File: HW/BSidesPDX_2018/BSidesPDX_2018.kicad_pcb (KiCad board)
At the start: 2 copper layers, 94.7 x 67.7 mm, 46 parts, among them J1 AVR-ISP-6, J2 USB_B_Micro, U1 ATTINY861-15XD, X1 Badgelife_shitty_connector, X2 Badgelife_shitty_connector, X3 Badgelife_shitty_connector, X4 Badgelife_shitty_connector

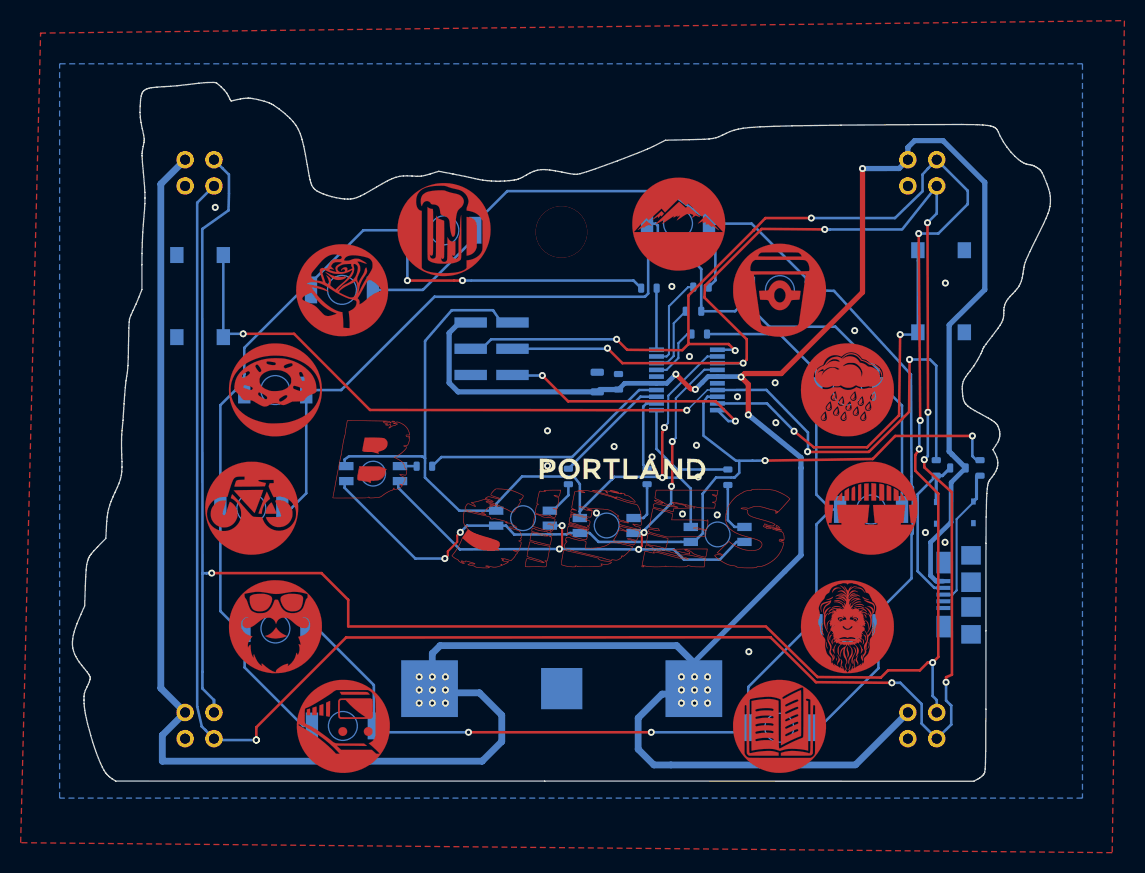
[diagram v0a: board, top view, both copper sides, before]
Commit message: BAD HACK: I edited the txt file of the LED footrpint, then updated all footprints in the schematic, then tweaked a few things. Someone competent should check this!
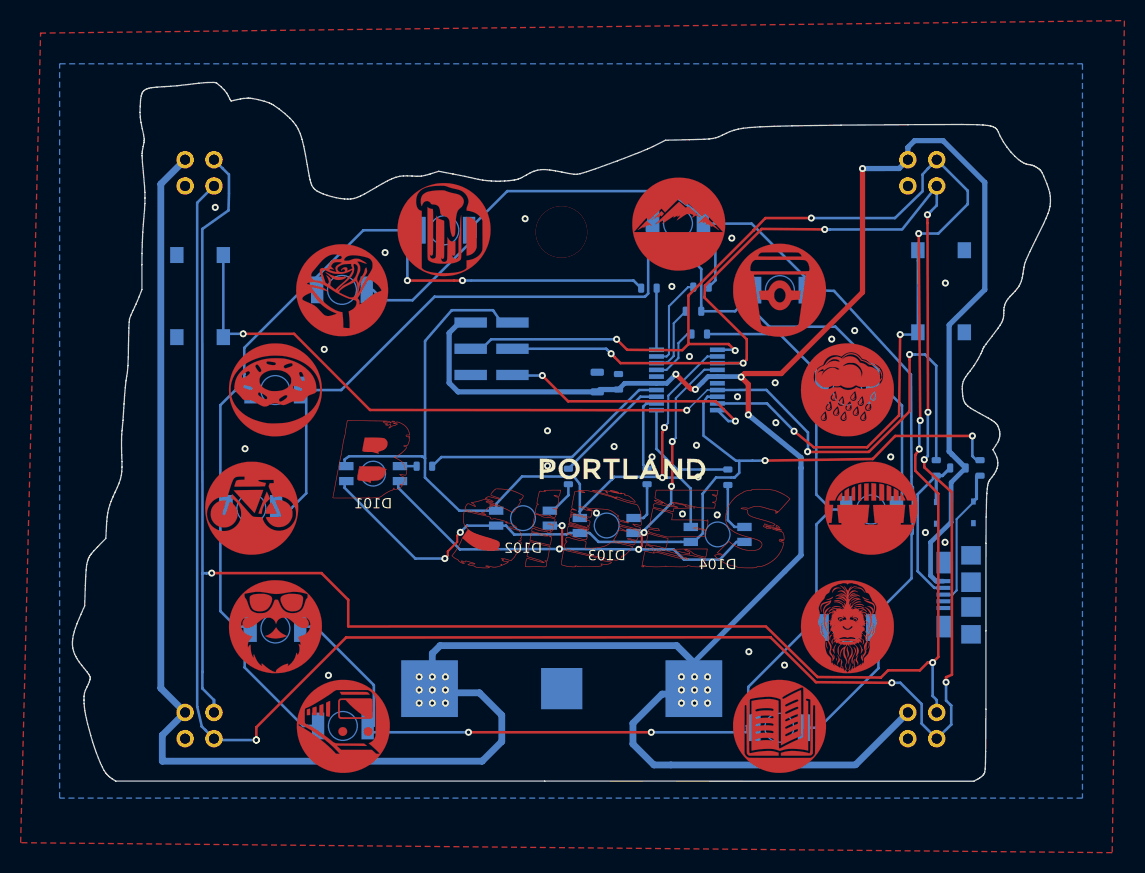
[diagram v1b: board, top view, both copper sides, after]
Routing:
- net /ROW_4: track 101.1 -> 102.3 mm
- net /ROW_2: track 109.7 -> 110.6 mm
- net /L_SWITCH_D-: track 100.8 -> 101.5 mm
- net GND: vias 20 -> 29

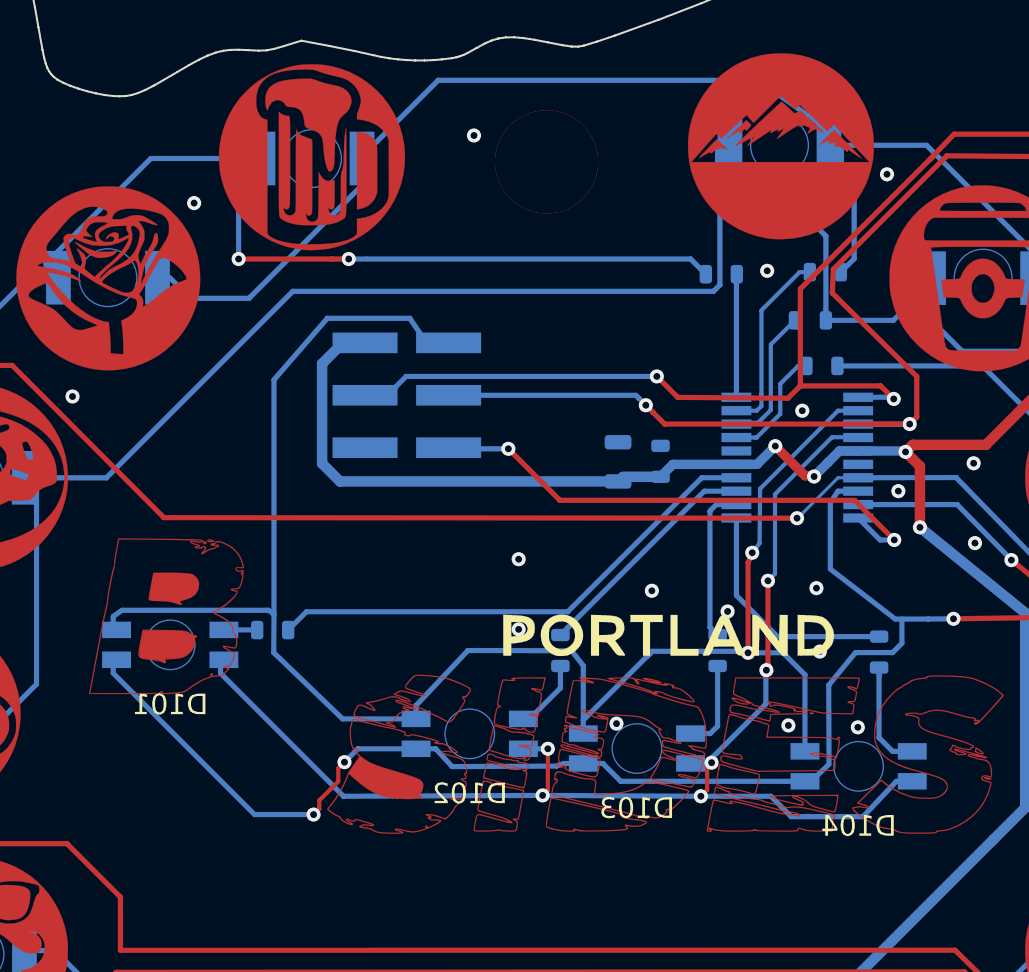
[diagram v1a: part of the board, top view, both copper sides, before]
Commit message: fixed RGB_LED sik layer. Updated layout, fixed one trace on D10
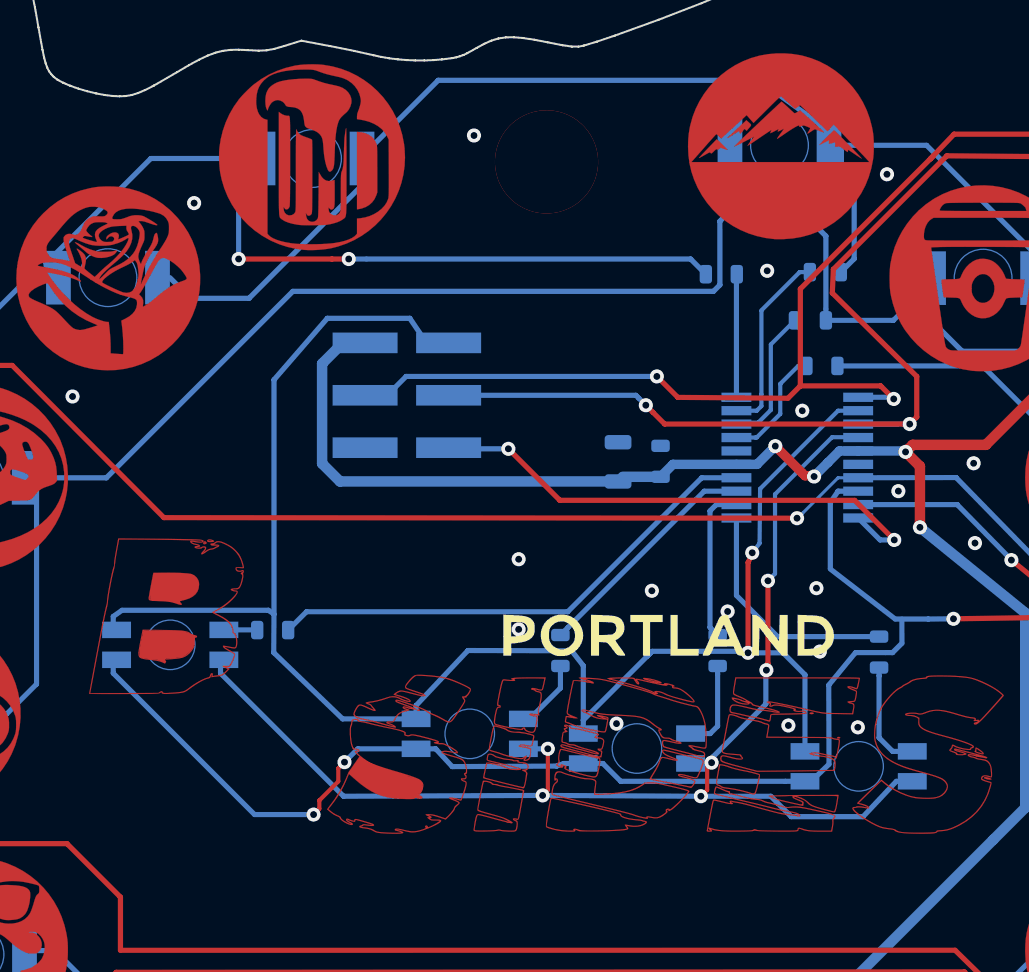
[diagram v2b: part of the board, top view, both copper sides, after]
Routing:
- net /ROW_3: track 107.6 -> 106.2 mm
